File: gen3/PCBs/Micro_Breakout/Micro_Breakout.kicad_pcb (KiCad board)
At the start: 2 copper layers, 123.5 x 83 mm, 50 parts, among them J1 BlueRobotics Depth Sensor, J10 Kill Switch, J11 StarOddi CTD Comms, J12 LED1, J13 LED2, J14 Leak Sensor, J15 Extra I2C #3, J16 Extra I2C #6, J17 Extra I2C #5, J18 Extra I2C #4, J19 GND Line, J2 Interconnect, J20 3.3V Line, J21 5V Line, J22 Extra SPI #1, J23 Extra SPI #2, J24 Extra SPI #3, J25 Secondary UART, J3 External Battery, J4 Conn_01x24, J5 External I2C, J6 Conn_01x24, J7 Extra I2C #1, J8 Extra I2C #2, J9 Lumen PWM, Q7 L78M05ABDT-TR, U15 AMS1117-3.3, U2 MCP9808_MSOP, U4 BME280, U6 Teensy4.1

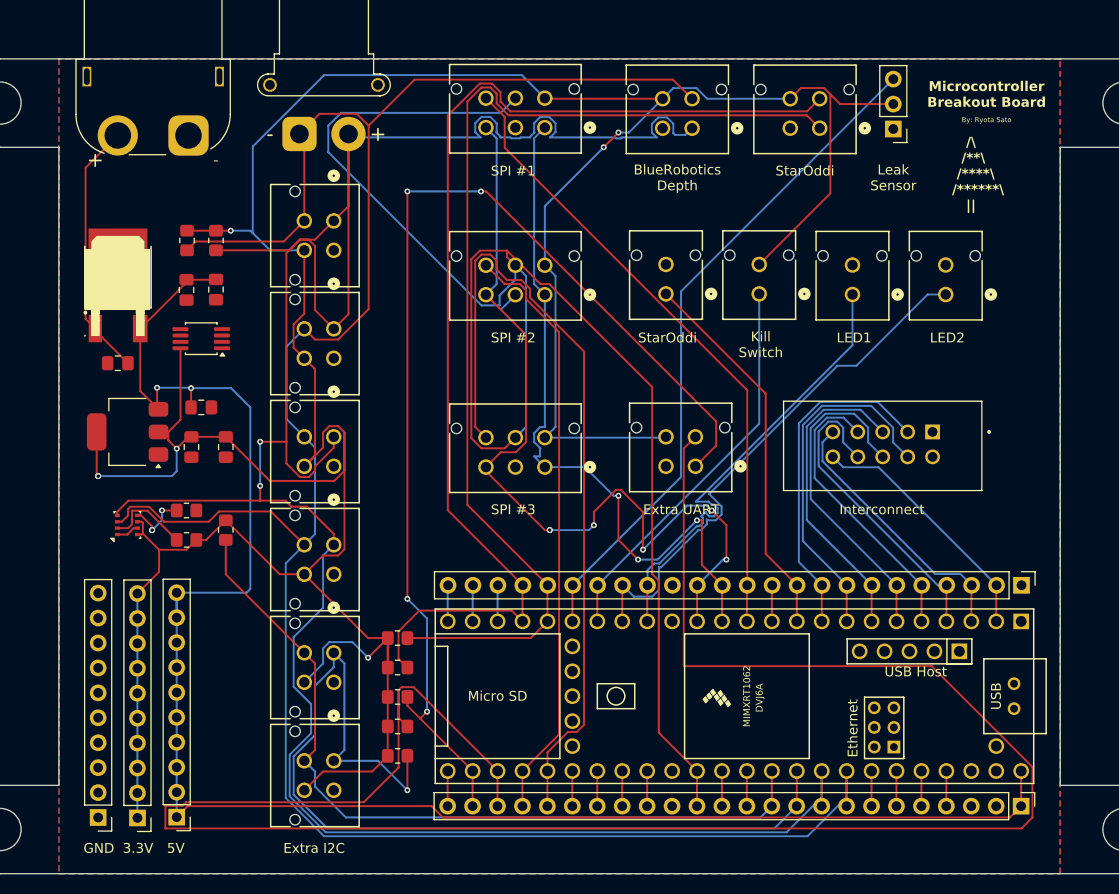
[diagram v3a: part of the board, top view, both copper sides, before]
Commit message: connected missing SDA SCL connection on gen 3 micro board
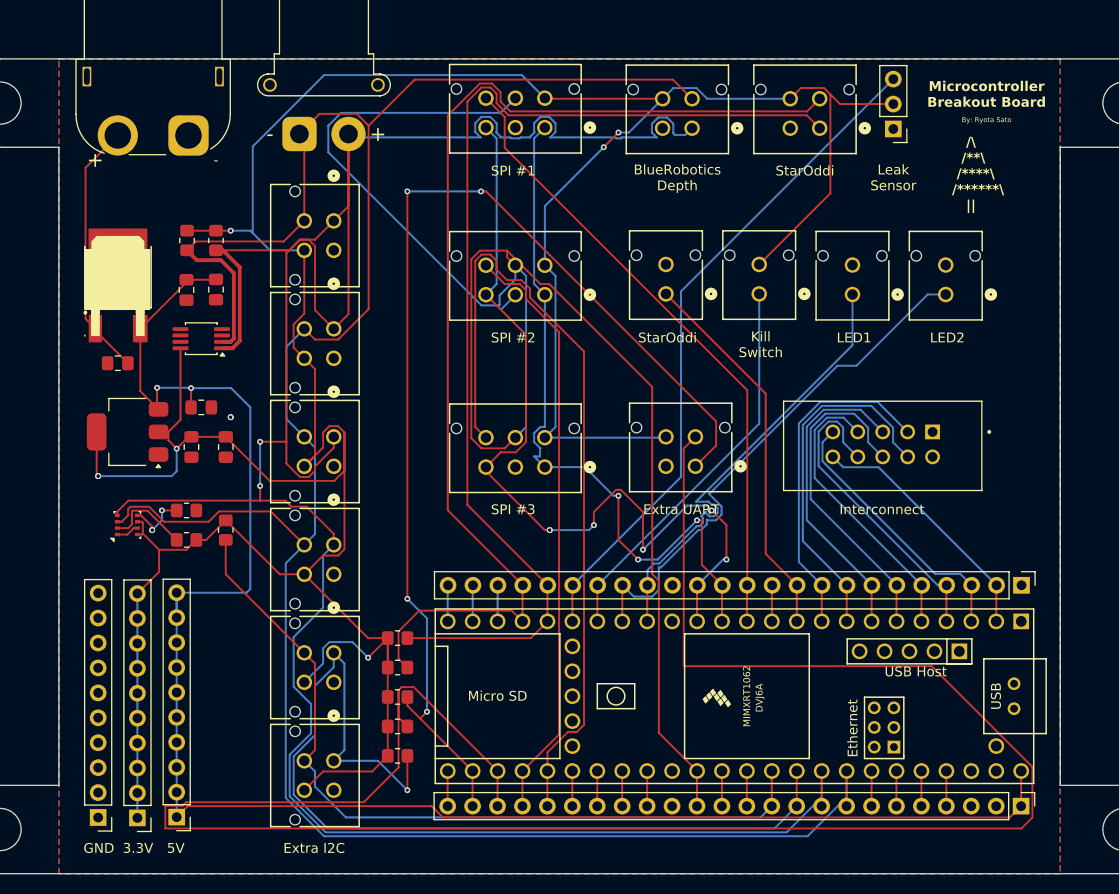
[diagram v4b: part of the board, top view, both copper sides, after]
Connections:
- U2 pad 1: unconnected-(U2-SDA-Pad1) -> I2C1_SDA
- U2 pad 2: unconnected-(U2-SCL-Pad2) -> I2C1_SCL
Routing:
- net I2C1_SCL: track 233.5 -> 247.2 mm
- net I2C1_SDA: track 259.3 -> 272.1 mm
- net GND: vias 0 -> 2
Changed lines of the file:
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@@
 	(net 52 "Net-(U4-CSB)")
 	(net 53 "unconnected-(U2-Alert-Pad3)")
-	(net 54 "unconnected-(U2-SDA-Pad1)")
-	(net 55 "unconnected-(U2-SCL-Pad2)")
-	(net 56 "unconnected-(U6-GND-Pad59)")
-	(net 57 "unconnected-(U6-VBAT-Pad50)")
-	(net 58 "unconnected-(U6-ON_OFF-Pad54)")
-	(net 59 "unconnected-(U6-GND-Pad52)")
-	(net 60 "unconnected-(U6-T+-Pad63)")
-	(net 61 "unconnected-(U6-PROGRAM-Pad53)")
-	(net 62 "unconnected-(U6-LED-Pad61)")
-	(net 63 "unconnected-(U6-D+-Pad67)")
-	(net 64 "unconnected-(U6-D+-Pad57)")
-	(net 65 "unconnected-(U6-5V-Pad55)")
-	(net 66 "unconnected-(U6-3V3-Pad15)")
-	(net 67 "unconnected-(U6-D--Pad56)")
-	(net 68 "unconnected-(U6-3V3-Pad51)")
-	(net 69 "unconnected-(U6-GND-Pad64)")
-	(net 70 "unconnected-(U6-R--Pad65)")
-	(net 71 "unconnected-(U6-3V3-Pad46)")
-	(net 72 "unconnected-(U6-GND-Pad58)")
-	(net 73 "unconnected-(U6-R+-Pad60)")
-	(net 74 "unconnected-(U6-T--Pad62)")
-	(net 75 "unconnected-(U6-VUSB-Pad49)")
-	(net 76 "unconnected-(U6-D--Pad66)")
+	(net 54 "unconnected-(U6-GND-Pad59)")
+	(net 55 "unconnected-(U6-VBAT-Pad50)")
+	(net 56 "unconnected-(U6-ON_OFF-Pad54)")
+	(net 57 "unconnected-(U6-GND-Pad52)")
+	(net 58 "unconnected-(U6-T+-Pad63)")
+	(net 59 "unconnected-(U6-PROGRAM-Pad53)")
+	(net 60 "unconnected-(U6-LED-Pad61)")
+	(net 61 "unconnected-(U6-D+-Pad67)")
+	(net 62 "unconnected-(U6-D+-Pad57)")
+	(net 63 "unconnected-(U6-5V-Pad55)")
+	(net 64 "unconnected-(U6-3V3-Pad15)")
+	(net 65 "unconnected-(U6-D--Pad56)")
+	(net 66 "unconnected-(U6-3V3-Pad51)")
+	(net 67 "unconnected-(U6-GND-Pad64)")
+	(net 68 "unconnected-(U6-R--Pad65)")
+	(net 69 "unconnected-(U6-3V3-Pad46)")
+	(net 70 "unconnected-(U6-GND-Pad58)")
+	(net 71 "unconnected-(U6-R+-Pad60)")
+	(net 72 "unconnected-(U6-T--Pad62)")
+	(net 73 "unconnected-(U6-VUSB-Pad49)")
+	(net 74 "unconnected-(U6-D--Pad66)")
 	(footprint "Imported_Footprints:CONN_SD-43045-005_04_MOL"
 		(layer "F.Cu")
@@
 			(layers "*.Cu" "*.Mask")
 			(remove_unused_layers no)
-			(net 66 "unconnected-(U6-3V3-Pad15)")
+			(net 64 "unconnected-(U6-3V3-Pad15)")
 			(pinfunction "3V3")
 			(pintype "power_in+no_connect")
@@
 			(layers "*.Cu" "*.Mask")
 			(remove_unused_layers no)
-			(net 71 "unconnected-(U6-3V3-Pad46)")
+			(net 69 "unconnected-(U6-3V3-Pad46)")
 			(pinfunction "3V3")
 			(pintype "output+no_connect")
@@
 			(layers "*.Cu" "*.Mask")
 			(remove_unused_layers no)
-			(net 75 "unconnected-(U6-VUSB-Pad49)")
+			(net 73 "unconnected-(U6-VUSB-Pad49)")
 			(pinfunction "VUSB")
 			(pintype "power_out+no_connect")
@@
 			(layers "*.Cu" "*.Mask")
 			(remove_unused_layers no)
-			(net 57 "unconnected-(U6-VBAT-Pad50)")
+			(net 55 "unconnected-(U6-VBAT-Pad50)")
 			(pinfunction "VBAT")
 			(pintype "power_in+no_connect")
@@
 			(layers "*.Cu" "*.Mask")
 			(remove_unused_layers no)
-			(net 68 "unconnected-(U6-3V3-Pad51)")
+			(net 66 "unconnected-(U6-3V3-Pad51)")
 			(pinfunction "3V3")
 			(pintype "power_in+no_connect")
@@
 			(layers "*.Cu" "*.Mask")
 			(remove_unused_layers no)
-			(net 59 "unconnected-(U6-GND-Pad52)")
+			(net 57 "unconnected-(U6-GND-Pad52)")
 			(pinfunction "GND")
 			(pintype "input+no_connect")
@@
 			(layers "*.Cu" "*.Mask")
 			(remove_unused_layers no)
-			(net 61 "unconnected-(U6-PROGRAM-Pad53)")
+			(net 59 "unconnected-(U6-PROGRAM-Pad53)")
 			(pinfunction "PROGRAM")
 			(pintype "input+no_connect")
@@
 			(layers "*.Cu" "*.Mask")
 			(remove_unused_layers no)
-			(net 58 "unconnected-(U6-ON_OFF-Pad54)")
+			(net 56 "unconnected-(U6-ON_OFF-Pad54)")
 			(pinfunction "ON_OFF")
 			(pintype "input+no_connect")
@@
 			(layers "*.Cu" "*.Mask")
 			(remove_unused_layers no)
-			(net 65 "unconnected-(U6-5V-Pad55)")
+			(net 63 "unconnected-(U6-5V-Pad55)")
 			(pinfunction "5V")
 			(pintype "power_out+no_connect")
@@
 			(layers "*.Cu" "*.Mask")
 			(remove_unused_layers no)
-			(net 67 "unconnected-(U6-D--Pad56)")
+			(net 65 "unconnected-(U6-D--Pad56)")
 			(pinfunction "D-")
 			(pintype "bidirectional+no_connect")
@@
 			(layers "*.Cu" "*.Mask")
 			(remove_unused_layers no)
-			(net 64 "unconnected-(U6-D+-Pad57)")
+			(net 62 "unconnected-(U6-D+-Pad57)")
 			(pinfunction "D+")
 			(pintype "bidirectional+no_connect")
@@
 			(layers "*.Cu" "*.Mask")
 			(remove_unused_layers no)
-			(net 72 "unconnected-(U6-GND-Pad58)")
+			(net 70 "unconnected-(U6-GND-Pad58)")
 			(pinfunction "GND")
 			(pintype "power_in+no_connect")
@@
 			(layers "*.Cu" "*.Mask")
 			(remove_unused_layers no)
-			(net 56 "unconnected-(U6-GND-Pad59)")
+			(net 54 "unconnected-(U6-GND-Pad59)")
 			(pinfunction "GND")
 			(pintype "power_in+no_connect")
@@
 			(layers "*.Cu" "*.Mask")
 			(remove_unused_layers no)
-			(net 73 "unconnected-(U6-R+-Pad60)")
+			(net 71 "unconnected-(U6-R+-Pad60)")
 			(pinfunction "R+")
 			(pintype "bidirectional+no_connect")
@@
 			(layers "*.Cu" "*.Mask")
 			(remove_unused_layers no)
-			(net 62 "unconnected-(U6-LED-Pad61)")
+			(net 60 "unconnected-(U6-LED-Pad61)")
 			(pinfunction "LED")
 			(pintype "bidirectional+no_connect")
@@
 			(layers "*.Cu" "*.Mask")
 			(remove_unused_layers no)
-			(net 74 "unconnected-(U6-T--Pad62)")
+			(net 72 "unconnected-(U6-T--Pad62)")
 			(pinfunction "T-")
 			(pintype "bidirectional+no_connect")
@@
 			(layers "*.Cu" "*.Mask")
 			(remove_unused_layers no)
-			(net 60 "unconnected-(U6-T+-Pad63)")
+			(net 58 "unconnected-(U6-T+-Pad63)")
 			(pinfunction "T+")
 			(pintype "bidirectional+no_connect")
@@
 			(layers "*.Cu" "*.Mask")
 			(remove_unused_layers no)
-			(net 69 "unconnected-(U6-GND-Pad64)")
+			(net 67 "unconnected-(U6-GND-Pad64)")
 			(pinfunction "GND")
 			(pintype "power_in+no_connect")
@@
 			(layers "*.Cu" "*.Mask")
 			(remove_unused_layers no)
-			(net 70 "unconnected-(U6-R--Pad65)")
+			(net 68 "unconnected-(U6-R--Pad65)")
 			(pinfunction "R-")
 			(pintype "bidirectional+no_connect")
@@
 			(layers "*.Cu" "*.Mask")
 			(remove_unused_layers no)
-			(net 76 "unconnected-(U6-D--Pad66)")
+			(net 74 "unconnected-(U6-D--Pad66)")
 			(pinfunction "D-")
 			(pintype "bidirectional+no_connect")
@@
 			(layers "*.Cu" "*.Mask")
 			(remove_unused_layers no)
-			(net 63 "unconnected-(U6-D+-Pad67)")
+			(net 61 "unconnected-(U6-D+-Pad67)")
 			(pinfunction "D+")
 			(pintype "bidirectional+no_connect")
@@
 			(layers "F.Cu" "F.Mask" "F.Paste")
 			(roundrect_rratio 0.25)
-			(net 54 "unconnected-(U2-SDA-Pad1)")
+			(net 6 "I2C1_SDA")
 			(pinfunction "SDA")
 			(pintype "bidirectional")
@@
 			(layers "F.Cu" "F.Mask" "F.Paste")
 			(roundrect_rratio 0.25)
-			(net 55 "unconnected-(U2-SCL-Pad2)")
+			(net 5 "I2C1_SCL")
 			(pinfunction "SCL")
 			(pintype "input")
@@
 		(net 2)
 	)
+	(via
+		(at 87.5 86.5)
+		(size 0.6)
+		(drill 0.3)
+		(layers "F.Cu" "B.Cu")
+		(free yes)
+		(net 2)
+	)
+	(via
+		(at 87.5 86.5)
+		(size 0.6)
+		(drill 0.3)
+		(layers "F.Cu" "B.Cu")
+		(free yes)
+		(net 2)
+	)
 	(segment
 		(start 116.500001 74.067099)
@@
 	)
 	(segment
+		(start 87.826 71.826)
+		(end 86.501 70.501)
+		(width 0.4)
+		(layer "F.Cu")
+		(net 5)
+	)
+	(segment
 		(start 101.551 56.800447)
 		(end 101.551 75.488231)
@@
 	)
 	(segment
+		(start 87.486292 78.825)
+		(end 87.826 78.485292)
+		(width 0.4)
+		(layer "F.Cu")
+		(net 5)
+	)
+	(segment
+		(start 86.6125 78.825)
+		(end 87.486292 78.825)
+		(width 0.4)
+		(layer "F.Cu")
+		(net 5)
+	)
+	(segment
 		(start 150.24 126.120595)
 		(end 150.24 122.548238)
@@
 	)
 	(segment
+		(start 86.501 70.501)
+		(end 84.051 70.501)
+		(width 0.4)
+		(layer "F.Cu")
+		(net 5)
+	)
+	(segment
 		(start 96.088401 78.5884)
 		(end 95.000001 77.5)
@@
 	)
 	(segment
+		(start 84.051 70.501)
+		(end 83.05 69.5)
+		(width 0.4)
+		(layer "F.Cu")
+		(net 5)
+	)
+	(segment
 		(start 100.349553 55.599)
 		(end 101.551 56.800447)
@@
 	)
 	(segment
+		(start 87.826 78.485292)
+		(end 87.826 71.826)
+		(width 0.4)
+		(layer "F.Cu")
+		(net 5)
+	)
+	(segment
 		(start 83.05 69.5)
 		(end 83.951 68.599)
@@
 	)
 	(segment
+		(start 88.427 78.734234)
+		(end 88.427 71.227)
+		(width 0.4)
+		(layer "F.Cu")
+		(net 6)
+	)
+	(segment
 		(start 96.088401 75.588401)
 		(end 96.088401 69.049168)
@@
 	)
 	(segment
+		(start 86.6125 79.475)
+		(end 87.686234 79.475)
+		(width 0.4)
+		(layer "F.Cu")
+		(net 6)
+	)
+	(segment
 		(start 93.077068 94.999)
 		(end 93.69367 95.615602)
@@
 	)
 	(segment
+		(start 87.686234 79.475)
+		(end 88.427 78.734234)
+		(width 0.4)
+		(layer "F.Cu")
+		(net 6)
+	)
+	(segment
 		(start 96.088401 91.52515)
 		(end 98 89.613551)
@@
 	)
 	(segment
+		(start 88.427 71.227)
+		(end 86.7 69.5)
+		(width 0.4)
+		(layer "F.Cu")
+		(net 6)
+	)
+	(segment
 		(start 99.5 57.65)
 		(end 99.5 76)
@@
 	)
 	(segment
+		(start 86.7 69.5)
+		(end 86 69.5)
+		(width 0.4)
+		(layer "F.Cu")
+		(net 6)
+	)
+	(segment
 		(start 90.5 94.999)
 		(end 93.077068 94.999)
@@
 		(polygon
 			(pts
-				(xy 70 50) (xy 70 133) (xy 172 133) (xy 172 50)
+				(xy 70 133) (xy 70 50) (xy 172 50) (xy 172 133)
 			)
 		)

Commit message: added all custom in robosub_3d_models
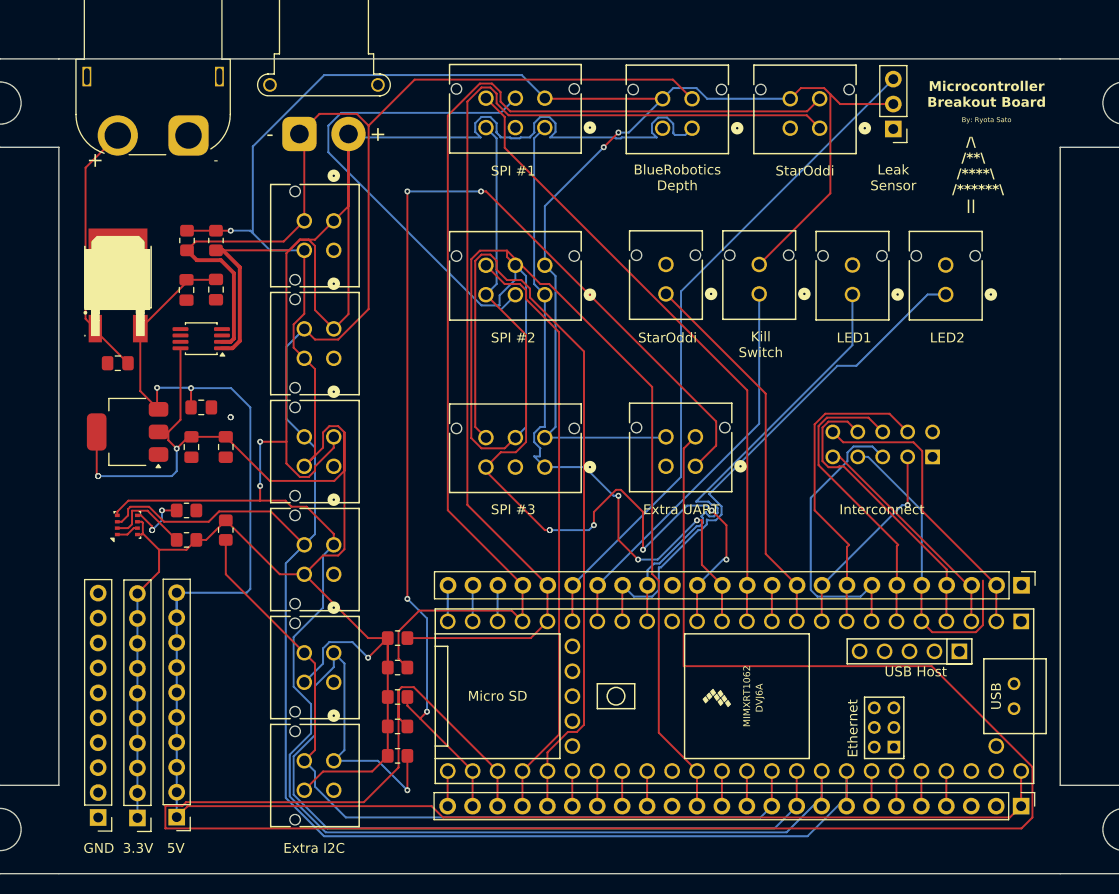
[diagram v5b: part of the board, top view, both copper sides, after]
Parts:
- J2: moved to B.Cu
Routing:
- net PWM7: track 34.4 -> 20.8 mm, vias 0 -> 1
- net PWM0: track 25.8 -> 30.4 mm
- net PWM1: track 27.5 -> 23.3 mm
- net PWM6: track 36.4 -> 32.3 mm
- net PWM4: track 34.0 -> 30.8 mm
- net PWM3: track 29.6 -> 31.8 mm
- net PWM2: track 32.1 -> 30.3 mm
- net PWM5: track 32.0 -> 30.5 mm
- removed copper zone on B.Cu, net GND
- removed copper zone on F.Cu, net GND

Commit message: works
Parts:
- removed R1: 0R, Resistor_SMD:R_0805_2012Metric_Pad1.20x1.40mm_HandSolder
- removed R2: 10k, Resistor_SMD:R_0805_2012Metric_Pad1.20x1.40mm_HandSolder
- removed U4: BME280, Package_LGA:Bosch_LGA-8_2.5x2.5mm_P0.65mm_ClockwisePinNumbering
- added U1: SHT31-DIS-B, robosub_footprints:DFN-8_L2.5-W2.5-P0.50-BL-EP, F.Cu at (6.57, 1.55)
- added U3: MS560702BA03-50, robosub_footprints:SENSOR-SMD_MS560702BA03-50, F.Cu at (2.46, 2.63)
- J1, J11, J15, J16, J17, J18, J25, J7, J8: footprint Imported_Footprints:CONN_SD-43045-005_04_MOL -> robosub_footprints:CONN_SD-43045-005_04_MOL
- J10, J12, J13, J9: footprint Imported_Footprints:CONN_SD-43045-005_02_MOL -> robosub_footprints:CONN_SD-43045-005_02_MOL
- J2: footprint Imported_Footprints:SULLINS_SBH11-PBPC-D05-ST-BK -> robosub_footprints:SULLINS_SBH11-PBPC-D05-ST-BK
- J22, J23, J24: footprint Imported_Footprints:CONN_SD-43045-005_06_MOL -> robosub_footprints:CONN_SD-43045-005_06_MOL
- U6: footprint Imported_Footprints:Teensy41 -> robosub_footprints:Teensy41
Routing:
- net (no net): track 0.00 -> 15.1 mm, vias 0 -> 3
- net Net-(U4-CSB): track 8.83 -> 0.00 mm
- net Net-(U4-SDO): track 6.25 -> 0.00 mm, vias 3 -> 0

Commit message: jlc_to_robosub working, and all parts are updated.
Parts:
- removed C12, C13: 10uF, Capacitor_SMD:C_0805_2012Metric_Pad1.18x1.45mm_HandSolder
- removed C14: 1uF, Capacitor_SMD:C_0805_2012Metric_Pad1.18x1.45mm_HandSolder
- removed U15: AMS1117-3.3, Package_TO_SOT_SMD:SOT-223-3_TabPin2
- removed U2: MCP9808_MSOP, Package_SO:MSOP-8_3x3mm_P0.65mm
- added C3: 10uF, Capacitor_SMD:C_0805_2012Metric_Pad1.18x1.45mm_HandSolder, F.Cu at (48.0, 70.6)
- added C4: 1uF, Capacitor_SMD:C_0805_2012Metric_Pad1.18x1.45mm_HandSolder, F.Cu at (48.0, 73.6)
- added C5: 10uF, Capacitor_SMD:C_0805_2012Metric_Pad1.18x1.45mm_HandSolder, F.Cu at (48.0, 76.6)
- added U4: AMS1117-3_3V_C5120796, robosub_footprints:SOT-89-3_L4.5-W2.5-P1.50-LS4.2-BR, F.Cu at (43.0, 73.1)
- added U5: MCP9808-E/MS, robosub_footprints:MSOP-8_L3.0-W3.0-P0.65-LS4.9-BL, F.Cu at (53.1, 72.6)
- moved U1 89.2 mm to (52.3, 78.1)
- moved U3 86.5 mm to (42.9, 79.1)
